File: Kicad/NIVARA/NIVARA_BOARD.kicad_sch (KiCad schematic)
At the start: 0 parts

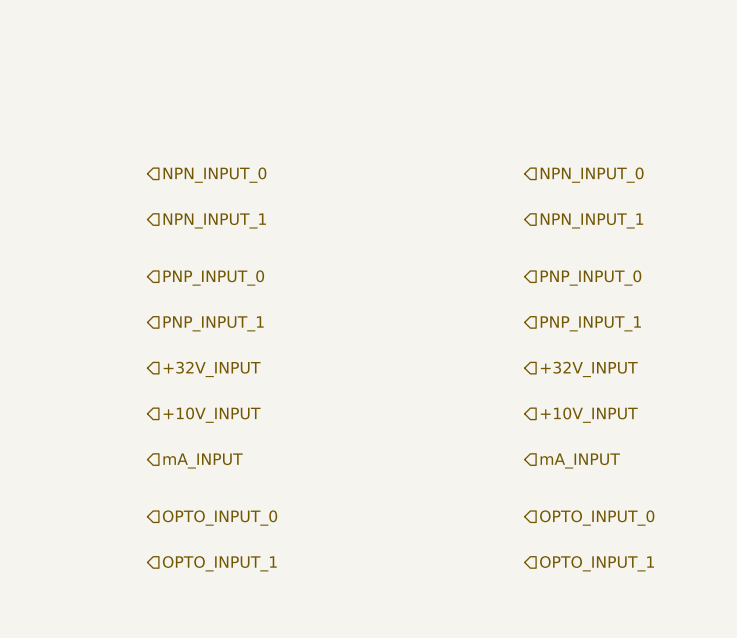
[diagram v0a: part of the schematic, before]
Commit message: Hierarchical Labels added
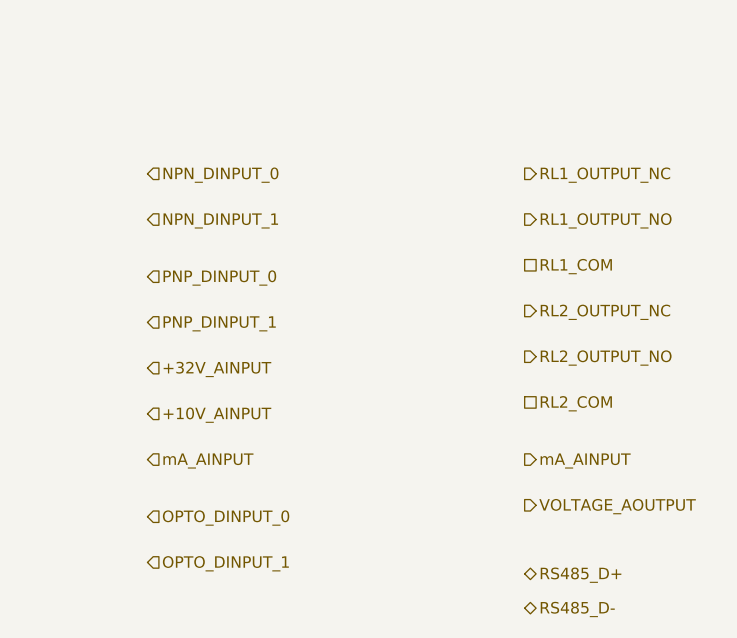
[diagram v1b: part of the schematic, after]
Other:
- company: (none) -> ELECTIVA ITLA
- title: (none) -> NIVARA
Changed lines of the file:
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@@
 	(generator "eeschema")
 	(generator_version "9.0")
-	(paper "A4")
-	(hierarchical_label "OPTO_INPUT_1"
+	(paper "USLedger")
+	(title_block
+		(title "NIVARA")
+		(date "2025-06-13")
+		(rev "1.0")
+		(company "ELECTIVA ITLA")
+	)
+	(hierarchical_label "OPTO_DINPUT_1"
 		(shape input)
 		(at 81.28 105.41 0)
@@
 		)
 	)
-	(hierarchical_label "OPTO_INPUT_1"
-		(shape input)
-		(at 123.19 105.41 0)
-		(effects
-			(font
-				(size 1.27 1.27)
-			)
-			(justify left)
-		)
-	)
-	(hierarchical_label "NPN_INPUT_1"
+	(hierarchical_label "NPN_DINPUT_1"
 		(shape input)
 		(at 81.28 67.31 0)
@@
 		)
 	)
-	(hierarchical_label "+10V_INPUT"
+	(hierarchical_label "+10V_AINPUT"
 		(shape input)
 		(at 81.28 88.9 0)
@@
 		)
 	)
-	(hierarchical_label "NPN_INPUT_0"
+	(hierarchical_label "NPN_DINPUT_0"
 		(shape input)
 		(at 81.28 62.23 0)
@@
 		)
 	)
-	(hierarchical_label "NPN_INPUT_0"
-		(shape input)
+	(hierarchical_label "RL1_OUTPUT_NC"
+		(shape output)
 		(at 123.19 62.23 0)
 		(effects
@@
 		)
 	)
-	(hierarchical_label "PNP_INPUT_0"
-		(shape input)
-		(at 123.19 73.66 0)
-		(effects
-			(font
-				(size 1.27 1.27)
-			)
-			(justify left)
-		)
-	)
-	(hierarchical_label "PNP_INPUT_0"
+	(hierarchical_label "PNP_DINPUT_0"
 		(shape input)
 		(at 81.28 73.66 0)
@@
 		)
 	)
-	(hierarchical_label "+32V_INPUT"
-		(shape input)
-		(at 123.19 83.82 0)
+	(hierarchical_label "RS485_D+"
+		(shape bidirectional)
+		(at 123.19 106.68 0)
 		(effects
 			(font
@@
 		)
 	)
-	(hierarchical_label "PNP_INPUT_1"
-		(shape input)
-		(at 123.19 78.74 0)
-		(effects
-			(font
-				(size 1.27 1.27)
-			)
-			(justify left)
-		)
-	)
-	(hierarchical_label "NPN_INPUT_1"
-		(shape input)
+	(hierarchical_label "RL1_OUTPUT_NO"
+		(shape output)
 		(at 123.19 67.31 0)
 		(effects
@@
 		)
 	)
-	(hierarchical_label "OPTO_INPUT_0"
+	(hierarchical_label "OPTO_DINPUT_0"
 		(shape input)
 		(at 81.28 100.33 0)
@@
 		)
 	)
-	(hierarchical_label "PNP_INPUT_1"
+	(hierarchical_label "PNP_DINPUT_1"
 		(shape input)
 		(at 81.28 78.74 0)
@@
 		)
 	)
-	(hierarchical_label "+10V_INPUT"
-		(shape input)
-		(at 123.19 88.9 0)
+	(hierarchical_label "RL2_COM"
+		(shape passive)
+		(at 123.19 87.63 0)
 		(effects
 			(font
@@
 		)
 	)
-	(hierarchical_label "OPTO_INPUT_0"
-		(shape input)
-		(at 123.19 100.33 0)
+	(hierarchical_label "VOLTAGE_AOUTPUT"
+		(shape output)
+		(at 123.19 99.06 0)
 		(effects
 			(font
@@
 		)
 	)
-	(hierarchical_label "mA_INPUT"
+	(hierarchical_label "RL1_COM"
+		(shape passive)
+		(at 123.19 72.39 0)
+		(effects
+			(font
+				(size 1.27 1.27)
+			)
+			(justify left)
+		)
+	)
+	(hierarchical_label "RS485_D-"
+		(shape bidirectional)
+		(at 123.19 110.49 0)
+		(effects
+			(font
+				(size 1.27 1.27)
+			)
+			(justify left)
+		)
+	)
+	(hierarchical_label "RL2_OUTPUT_NO"
+		(shape output)
+		(at 123.19 82.55 0)
+		(effects
+			(font
+				(size 1.27 1.27)
+			)
+			(justify left)
+		)
+	)
+	(hierarchical_label "mA_AINPUT"
 		(shape input)
 		(at 81.28 93.98 0)
@@
 		)
 	)
-	(hierarchical_label "+32V_INPUT"
+	(hierarchical_label "RL2_OUTPUT_NC"
+		(shape output)
+		(at 123.19 77.47 0)
+		(effects
+			(font
+				(size 1.27 1.27)
+			)
+			(justify left)
+		)
+	)
+	(hierarchical_label "+32V_AINPUT"
 		(shape input)
 		(at 81.28 83.82 0)
@@
 		)
 	)
-	(hierarchical_label "mA_INPUT"
-		(shape input)
+	(hierarchical_label "mA_AINPUT"
+		(shape output)
 		(at 123.19 93.98 0)
 		(effects

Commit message: Initial Capture Finished
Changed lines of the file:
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@@
+		)
+	)
+	(hierarchical_label "PNP_DOUTPUT_1"
+		(shape output)
+		(at 123.19 133.35 0)
+		(effects
+			(font
+				(size 1.27 1.27)
+			)
+			(justify left)
 		)
 	)
@@
 		)
 	)
+	(hierarchical_label "~{RUN}{slash}STOP"
+		(shape input)
+		(at 81.28 109.22 0)
+		(effects
+			(font
+				(size 1.27 1.27)
+			)
+			(justify left)
+		)
+	)
 	(hierarchical_label "NPN_DINPUT_0"
 		(shape input)
@@
 		)
 	)
+	(hierarchical_label "PNP_DOUTPUT_0"
+		(shape output)
+		(at 123.19 128.27 0)
+		(effects
+			(font
+				(size 1.27 1.27)
+			)
+			(justify left)
+		)
+	)
 	(hierarchical_label "RL1_OUTPUT_NC"
 		(shape output)
@@
 		)
 	)
-	(hierarchical_label "RS485_D+"
+	(hierarchical_label "RS485_A"
 		(shape bidirectional)
 		(at 123.19 106.68 0)
@@
 		)
 	)
-	(hierarchical_label "RS485_D-"
+	(hierarchical_label "RS485_B"
 		(shape bidirectional)
-		(at 123.19 110.49 0)
+		(at 123.19 111.76 0)
+		(effects
+			(font
+				(size 1.27 1.27)
+			)
+			(justify left)
+		)
+	)
+	(hierarchical_label "NPN_DOUTPUT_0"
+		(shape output)
+		(at 123.19 116.84 0)
 		(effects
 			(font
@@
 		)
 	)
+	(hierarchical_label "NPN_DOUTPUT_1"
+		(shape output)
+		(at 123.19 121.92 0)
+		(effects
+			(font
+				(size 1.27 1.27)
+			)
+			(justify left)
+		)
+	)
 	(hierarchical_label "RL2_OUTPUT_NC"
 		(shape output)
@@
 		)
 	)
-	(hierarchical_label "mA_AINPUT"
+	(hierarchical_label "mA_AOUTPUT"
 		(shape output)
 		(at 123.19 93.98 0)

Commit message: Wrapping up for today :3
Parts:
- added C1: C, symbol Device:C
- added R1: R, symbol Device:R
- added U1: ESP32-S3-WROOM-1, PCM_Espressif:ESP32-S3-WROOM-1, symbol PCM_Espressif:ESP32-S3-WROOM-1
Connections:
- new net: C1.1, R1.2, U1.3 (EN)
- new net +3.3V: R1.1, U1.2 (3V3)
- new net GND: C1.2, U1.1 (GND), U1.40 (GND), U1.41 (GND)
- new net RS485_INTERFACE/UART_IN: U1.37 (U0TXD/GPIO43/CLK_OUT1)
- new net RS485_INTERFACE/UART_OUT: U1.36 (U0RXD/GPIO44/CLK_OUT2)
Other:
- added sheet RS485_INTERFACE (RS485_INTERFACE.kicad_sch)

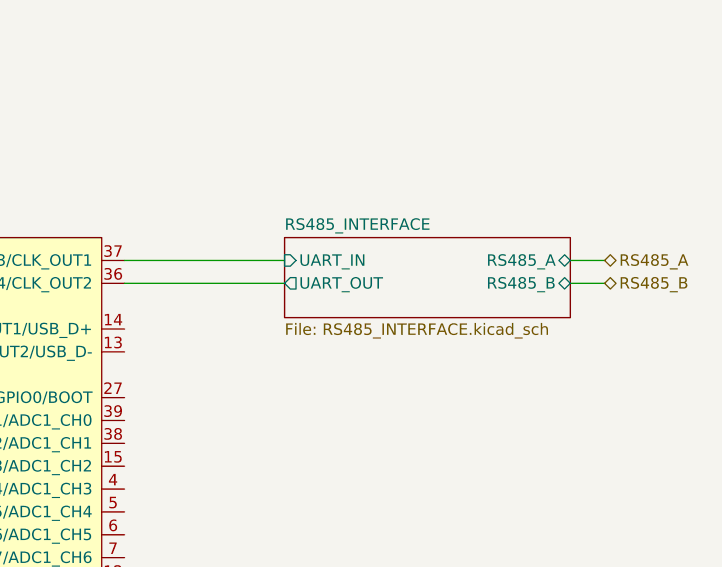
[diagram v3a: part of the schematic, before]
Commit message: RS-485 Update
RS-485 Isolated circuit updated. Created new symbol and footprint for the YLPTEC RSM3485ECHT IC.
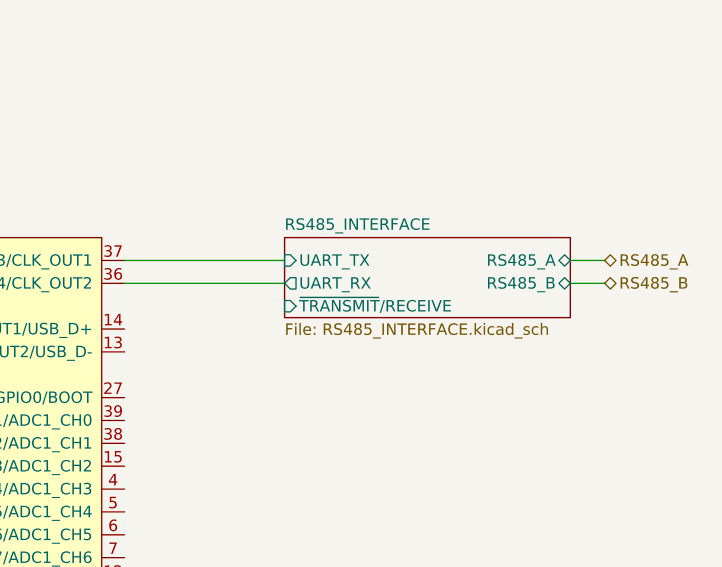
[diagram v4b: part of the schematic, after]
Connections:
- net RS485_INTERFACE/UART_IN renamed RS485_INTERFACE/UART_TX
- net RS485_INTERFACE/UART_OUT renamed RS485_INTERFACE/UART_RX
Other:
- sheet RS485_INTERFACE ports: added UART_RX, UART_TX, ~{TRANSMIT}/RECEIVE; removed UART_IN, UART_OUT
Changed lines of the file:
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@@
 			)
 		)
-		(pin "UART_IN" input
+		(pin "UART_TX" input
 			(at 278.13 64.77 180)
 			(effects
@@
 			)
 		)
-		(pin "UART_OUT" output
+		(pin "UART_RX" output
 			(at 278.13 67.31 180)
 			(effects
 				(font
+					(size 1.27 1.27)
+				)
+				(justify left)
+			)
+		)
+		(pin "~{TRANSMIT}{slash}RECEIVE" input
+			(at 278.13 69.85 180)
+			(effects
+				(font

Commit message: Relay Interface
Progress made with the Relay Interface.
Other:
- added sheet RELAY_INTERFACE (RELAY_INTERFACE.kicad_sch)
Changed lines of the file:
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@@
+	(wire
+		(pts
+			(xy 328.93 107.95) (xy 332.74 107.95)
+		)
+		(stroke
+			(width 0)
+			(type default)
+		)
+	)
 	(wire
 		(pts
@@
 	(wire
 		(pts
+			(xy 328.93 97.79) (xy 332.74 97.79)
+		)
+		(stroke
+			(width 0)
+			(type default)
+		)
+	)
+	(wire
+		(pts
 			(xy 160.02 64.77) (xy 165.1 64.77)
 		)
@@
 	(wire
 		(pts
+			(xy 328.93 87.63) (xy 332.74 87.63)
+		)
+		(stroke
+			(width 0)
+			(type default)
+		)
+	)
+	(wire
+		(pts
 			(xy 309.88 67.31) (xy 313.69 67.31)
 		)
@@
 	(wire
 		(pts
+			(xy 328.93 92.71) (xy 332.74 92.71)
+		)
+		(stroke
+			(width 0)
+			(type default)
+		)
+	)
+	(wire
+		(pts
+			(xy 328.93 113.03) (xy 332.74 113.03)
+		)
+		(stroke
+			(width 0)
+			(type default)
+		)
+	)
+	(wire
+		(pts
 			(xy 260.35 67.31) (xy 278.13 67.31)
+		)
+		(stroke
+			(width 0)
+			(type default)
+		)
+	)
+	(wire
+		(pts
+			(xy 328.93 102.87) (xy 332.74 102.87)
 		)
 		(stroke
@@
 	(hierarchical_label "RL1_OUTPUT_NC"
 		(shape output)
-		(at 123.19 62.23 0)
+		(at 332.74 87.63 0)
 		(effects
 			(font
@@
 	(hierarchical_label "RL1_OUTPUT_NO"
 		(shape output)
-		(at 123.19 67.31 0)
+		(at 332.74 92.71 0)
 		(effects
 			(font
@@
 	(hierarchical_label "RL2_COM"
 		(shape passive)
-		(at 123.19 87.63 0)
+		(at 332.74 113.03 0)
 		(effects
 			(font
@@
 	(hierarchical_label "RL1_COM"
 		(shape passive)
-		(at 123.19 72.39 0)
+		(at 332.74 97.79 0)
 		(effects
 			(font
@@
 	(hierarchical_label "RL2_OUTPUT_NO"
 		(shape output)
-		(at 123.19 82.55 0)
+		(at 332.74 107.95 0)
 		(effects
 			(font
@@
 	(hierarchical_label "RL2_OUTPUT_NC"
 		(shape output)
-		(at 123.19 77.47 0)
+		(at 332.74 102.87 0)
 		(effects
 			(font
@@
 				)
 			)
+		)
+	)
+	(sheet
+		(at 295.91 85.09)
+		(size 33.02 30.48)
+		(exclude_from_sim no)
+		(in_bom yes)
+		(on_board yes)
+		(dnp no)
+		(fields_autoplaced yes)
+		(stroke
+			(width 0.1524)
+			(type solid)
+		)
+		(fill
+			(color 0 0 0 0.0000)
+		)
+		(property "Sheetname" "RELAY_INTERFACE"
+			(at 295.91 84.3784 0)
+			(effects
+				(font
+					(size 1.27 1.27)
+				)
+				(justify left bottom)
+			)
+		)
+		(property "Sheetfile" "RELAY_INTERFACE.kicad_sch"
+			(at 295.91 116.1546 0)
+			(effects
+				(font
+					(size 1.27 1.27)
+				)
+				(justify left top)
+			)
+		)
+		(pin "RL1_COM" passive
+			(at 328.93 97.79 0)
+			(effects
+				(font
+					(size 1.27 1.27)
+				)
+				(justify right)
+			)
+		)
+		(pin "RL1_EN" input
+			(at 295.91 92.71 180)
+			(effects
+				(font
+					(size 1.27 1.27)
+				)
+				(justify left)
+			)
+		)
+		(pin "RL1_OUTPUT_NC" output
+			(at 328.93 87.63 0)
+			(effects
+				(font
+					(size 1.27 1.27)
+				)
+				(justify right)
+			)
+		)
+		(pin "RL1_OUTPUT_NO" output
+			(at 328.93 92.71 0)
+			(effects
+				(font
+					(size 1.27 1.27)
+				)
+				(justify right)
+			)
+		)
+		(pin "RL2_COM" passive
+			(at 328.93 113.03 0)
+			(effects
+				(font
+					(size 1.27 1.27)
+				)
+				(justify right)
+			)
+		)
+		(pin "RL2_EN" input
+			(at 295.91 107.95 180)
+			(effects
+				(font
+					(size 1.27 1.27)
+				)
+				(justify left)
+			)
+		)
+		(pin "RL2_OUTPUT_NC" output
+			(at 328.93 102.87 0)
+			(effects
+				(font
+					(size 1.27 1.27)
+				)
+				(justify right)
+			)
+		)
+		(pin "RL2_OUTPUT_NO" output
+			(at 328.93 107.95 0)
+			(effects
+				(font
+					(size 1.27 1.27)
+				)
+				(justify right)
+			)
+		)
+		(pin "ST1" output
+			(at 295.91 95.25 180)
+			(effects
+				(font
+					(size 1.27 1.27)
+				)
+				(justify left)
+			)
+		)
+		(pin "ST2" output
+			(at 295.91 110.49 180)
+			(effects
+				(font
+					(size 1.27 1.27)
+				)
+				(justify left)
+			)
+		)
+		(instances
+			(project "NIVARA"
+				(path "/8290cc18-06d0-4e02-a781-29a61ebc321a/9e4d7a0c-a5eb-4e88-9036-0c35e68b279a"
+					(page "5")
+				)
+			)
